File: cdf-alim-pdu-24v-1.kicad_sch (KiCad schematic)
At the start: 133 parts, among them J1 Conn_01x02, J10 Conn_01x02, J11 Conn_01x02, J12 Conn_01x02, J13 Conn_01x02, J14 Conn_01x02, J15 Conn_01x02, J16 Conn_01x02, J17 Conn_01x02, J18 Conn_01x02, J19 Conn_01x02, J3 Conn_01x02, J5 Conn_01x02, J6 Conn_01x02, J7 Conn_01x02, J8 Conn_01x02, J9 Conn_01x02, Q3 BSC019N04LS, Q4 BSC019N04LS, Q5 BSC019N04LS, U1 HT753-1, U2 TPS25983, U3 TPS25983, U4 TPS25983, U5 MX25947, U6 MX25947, U7 MX25947

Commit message: schem: remove handsolder footprints
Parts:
- C10, C13, C17: footprint Capacitor_SMD:C_0603_1608Metric_Pad1.08x0.95mm_HandSolder -> Capacitor_SMD:C_0603_1608Metric
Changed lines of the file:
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@@
 			)
 		)
-		(property "Footprint" "Capacitor_SMD:C_0603_1608Metric_Pad1.08x0.95mm_HandSolder"
+		(property "Footprint" "Capacitor_SMD:C_0603_1608Metric"
 			(at 101.9048 95.25 0)
 			(hide yes)
@@
 			)
 		)
-		(property "Footprint" "Capacitor_SMD:C_0603_1608Metric_Pad1.08x0.95mm_HandSolder"
+		(property "Footprint" "Capacitor_SMD:C_0603_1608Metric"
 			(at 100.6348 38.1 0)
 			(hide yes)
@@
 			)
 		)
-		(property "Footprint" "Capacitor_SMD:C_0603_1608Metric_Pad1.08x0.95mm_HandSolder"
+		(property "Footprint" "Capacitor_SMD:C_0603_1608Metric"
 			(at 101.9048 153.67 0)
 			(hide yes)

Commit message: schem: add title
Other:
- company: (none) -> Rémi Ait-Younes
- title: (none) -> CDF Alim PDU 24V 1
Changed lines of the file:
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@@
 	(generator_version "10.0")
 	(paper "A4")
+	(title_block
+		(title "CDF Alim PDU 24V 1")
+		(date "2026-10-11")
+		(rev "01")
+		(company "Rémi Ait-Younes")
+	)
 	(rectangle
 		(start 148.59 97.79)

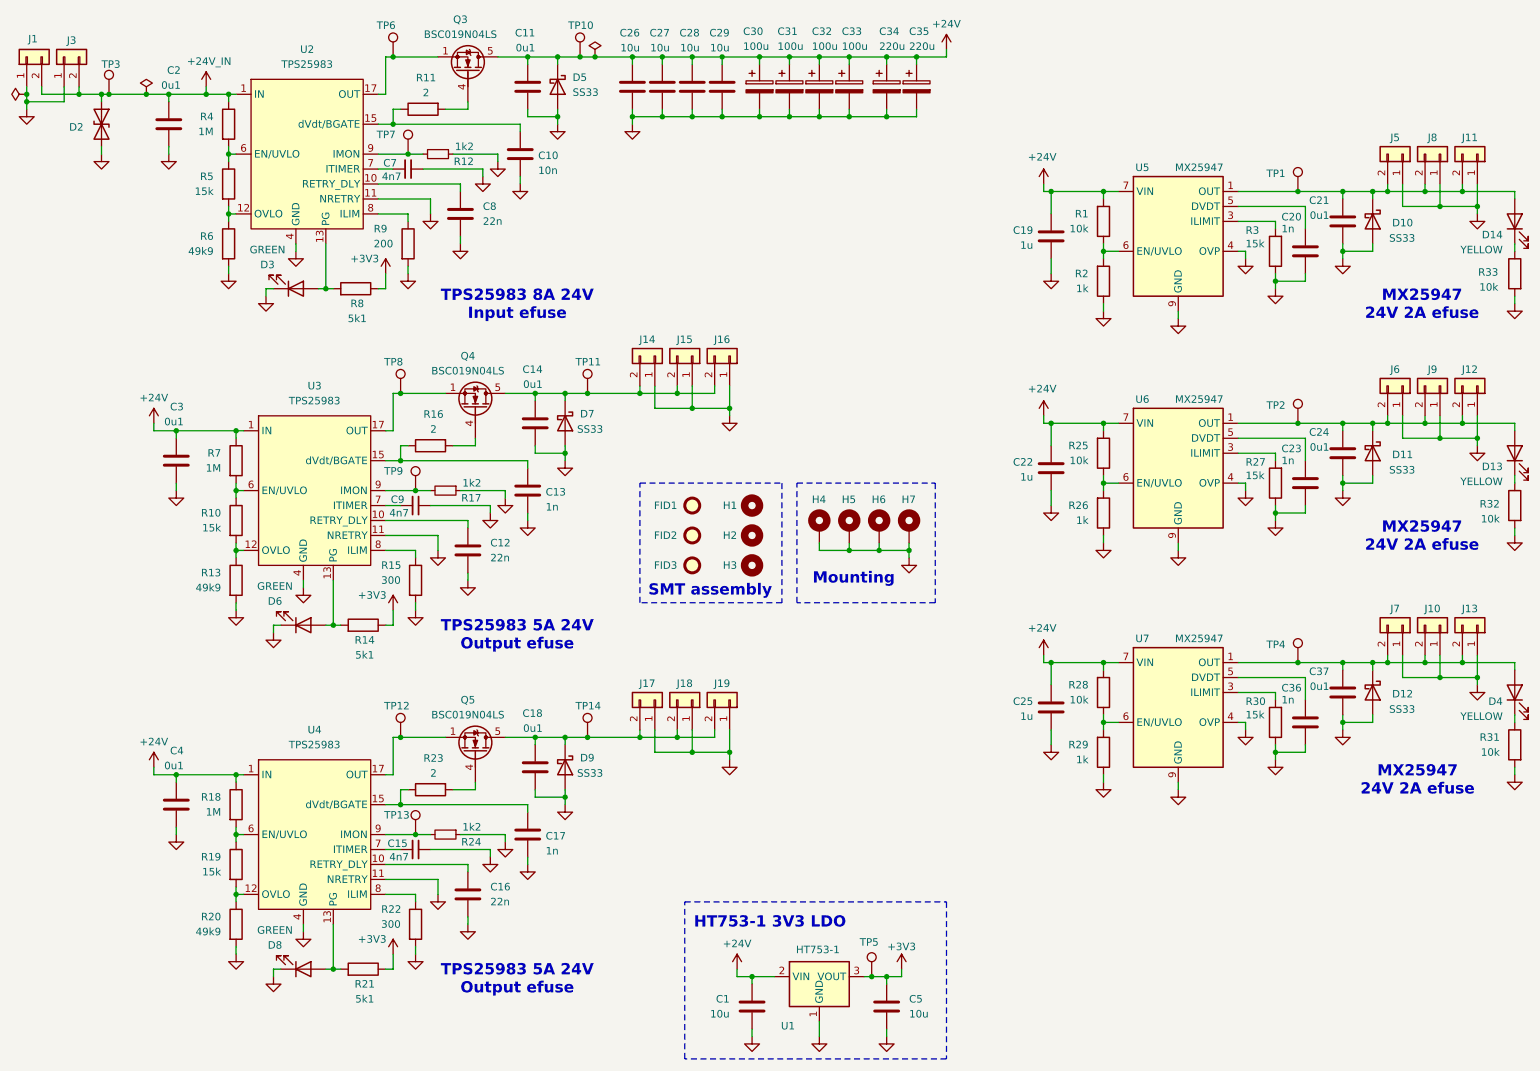
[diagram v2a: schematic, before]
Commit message: schem: renumber
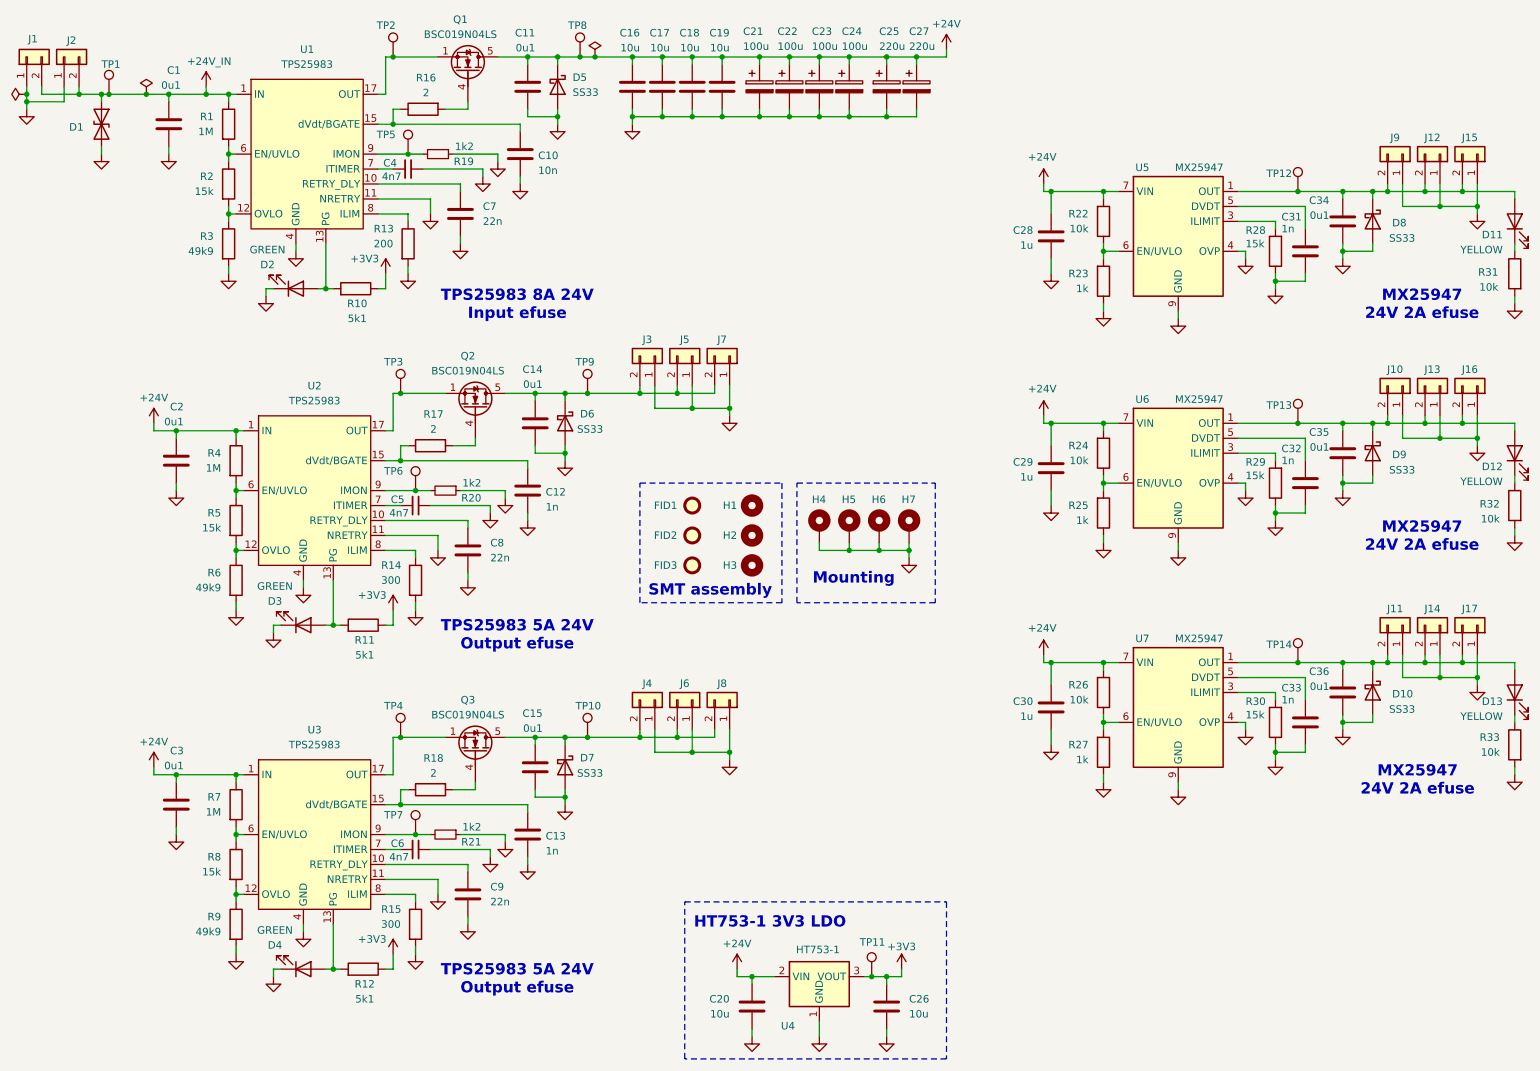
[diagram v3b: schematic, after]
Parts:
- renumbered C2 to C1, C13 to C12, C17 to C13, C18 to C15, C26 to C16, C27 to C17, C28 to C18, C29 to C19, C3 to C2, C1 to C20, C30 to C21, C31 to C22, C32 to C23, C33 to C24, C34 to C25, C5 to C26, C35 to C27, C19 to C28, C22 to C29, C4 to C3, C25 to C30, C20 to C31, C23 to C32, C36 to C33, C21 to C34, C24 to C35, C37 to C36, C7 to C4, C9 to C5, C15 to C6, C8 to C7, C12 to C8, C16 to C9, D2 to D1, D12 to D10, D14 to D11, D13 to D12, D4 to D13, D3 to D2, D6 to D3, D8 to D4, D7 to D6, D9 to D7, D10 to D8, D11 to D9, J6 to J10, J7 to J11, J8 to J12, J9 to J13, J10 to J14, J11 to J15, J12 to J16, J13 to J17, J3 to J2, J14 to J3, J17 to J4, J15 to J5, J18 to J6, J16 to J7, J19 to J8, J5 to J9, Q3 to Q1, Q4 to Q2, Q5 to Q3, R4 to R1, R8 to R10, R14 to R11, R21 to R12, R9 to R13, R15 to R14, R22 to R15, R11 to R16, R16 to R17, R23 to R18, R12 to R19, R5 to R2, R17 to R20, R24 to R21, R1 to R22, R2 to R23, R25 to R24, R26 to R25, R28 to R26, R29 to R27, R3 to R28, R27 to R29, R6 to R3, R33 to R31, R31 to R33, R7 to R4, R10 to R5, R13 to R6, R18 to R7, R19 to R8, R20 to R9, TP3 to TP1, TP14 to TP10, TP5 to TP11, TP1 to TP12, TP2 to TP13, TP4 to TP14, TP6 to TP2, TP8 to TP3, TP12 to TP4, TP7 to TP5, TP9 to TP6, TP13 to TP7, TP10 to TP8, TP11 to TP9, U2 to U1, U3 to U2, U4 to U3, U1 to U4

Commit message: schem: remove extra test points
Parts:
- removed TP10, TP8, TP9: TestPoint, TestPoint:TestPoint_Pad_D2.0mm, symbol Connector:TestPoint

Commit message: schem: add +24v testpoint
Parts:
- added TP8: TestPoint, TestPoint:TestPoint_Pad_D2.0mm, symbol Connector:TestPoint
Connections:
- net +24V: now also TP8.1
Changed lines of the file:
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@@
 	)
 	(junction
+		(at 172.72 25.4)
+		(diameter 0)
+		(color 0 0 0 0)
+	)
+	(junction
 		(at 128.27 140.97)
 		(diameter 0)
@@
 	(wire
 		(pts
-			(xy 173.99 25.4) (xy 168.91 25.4)
+			(xy 173.99 25.4) (xy 172.72 25.4)
 		)
 		(stroke
@@
 	(wire
 		(pts
+			(xy 172.72 25.4) (xy 168.91 25.4)
+		)
+		(stroke
+			(width 0)
+			(type default)
+		)
+	)
+	(wire
+		(pts
 			(xy 157.48 25.4) (xy 157.48 26.67)
 		)
@@
 					(unit 1)
 				)
+			)
+		)
+	)
+	(symbol
+		(lib_id "Connector:TestPoint")
+		(at 172.72 25.4 180)
+		(unit 1)
+		(body_style 1)
+		(exclude_from_sim no)
+		(in_bom no)
+		(on_board yes)
+		(in_pos_files yes)
+		(dnp no)
+		(property "Reference" "TP8"
+			(at 177.546 28.956 0)
+			(show_name no)
+			(do_not_autoplace no)
+			(effects
+				(font
+					(size 1.27 1.27)
+				)
+				(justify left)
+			)
+		)
+		(property "Value" "TestPoint"
+			(at 170.18 27.4321 0)
+			(hide yes)
+			(show_name no)
+			(do_not_autoplace no)
+			(effects
+				(font
+					(size 1.27 1.27)
+				)
+				(justify left)
+			)
+		)
+		(property "Footprint" "TestPoint:TestPoint_Pad_D2.0mm"
+			(at 167.64 25.4 0)
+			(hide yes)
+			(show_name no)
+			(do_not_autoplace no)
+			(effects
+				(font
+					(size 1.27 1.27)
+				)
+			)
+		)
+		(property "Datasheet" ""
+			(at 167.64 25.4 0)
+			(hide yes)
+			(show_name no)
+			(do_not_autoplace no)
+			(effects
+				(font
+					(size 1.27 1.27)
+				)
+			)
+		)
+		(property "Description" "test point"
+			(at 172.72 25.4 0)
+			(hide yes)
+			(show_name no)
+			(do_not_autoplace no)
+			(effects
+				(font
+					(size 1.27 1.27)
+				)
+			)
+		)
+		(pin "1"
+		)
+		(instances
+			(project "cdf-alim-pdu-24v-1"
+				(path "/3f2c4a1d-ccb4-4431-a881-d21d84b5ce46"
+					(reference "TP8")
+					(unit 1)
+				)
